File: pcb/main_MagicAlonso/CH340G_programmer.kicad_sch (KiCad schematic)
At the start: 13 parts, among them J2 USB_Out, J3 UART_Out, J4 USB_C_Receptacle_USB2.0_16P, Q1 NMOS, U4 CH340C

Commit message: schematic and test commit
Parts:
- D6: value 1N5819 -> SS14
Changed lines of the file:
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@@
 			)
 		)
-		(property "Value" "1N5819"
+		(property "Value" "SS14"
 			(at 91.694 26.67 0)
 			(effects

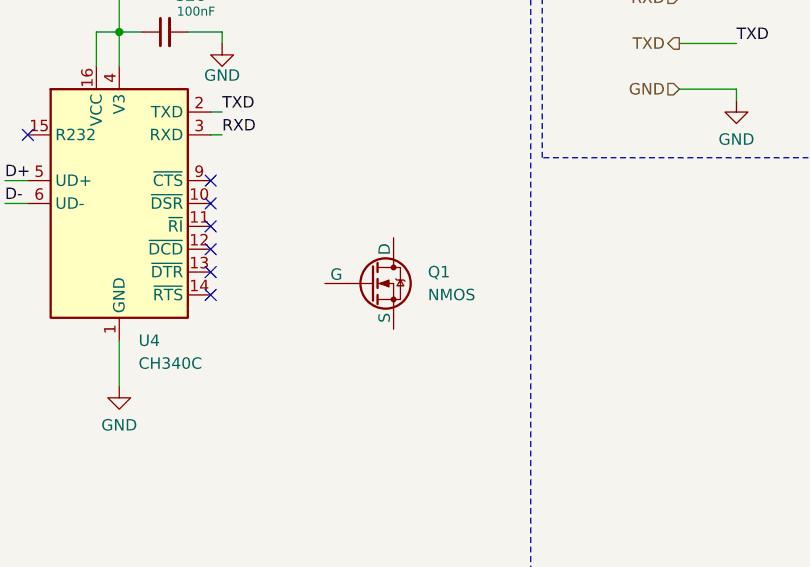
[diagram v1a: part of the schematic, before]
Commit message: Big changes PCB
Advancements on the schematic were made:
- Completed MP2315 circuit
- Passive Buzzer
- Mounting holes & other symbols added

Also the PCB drawings were improved.
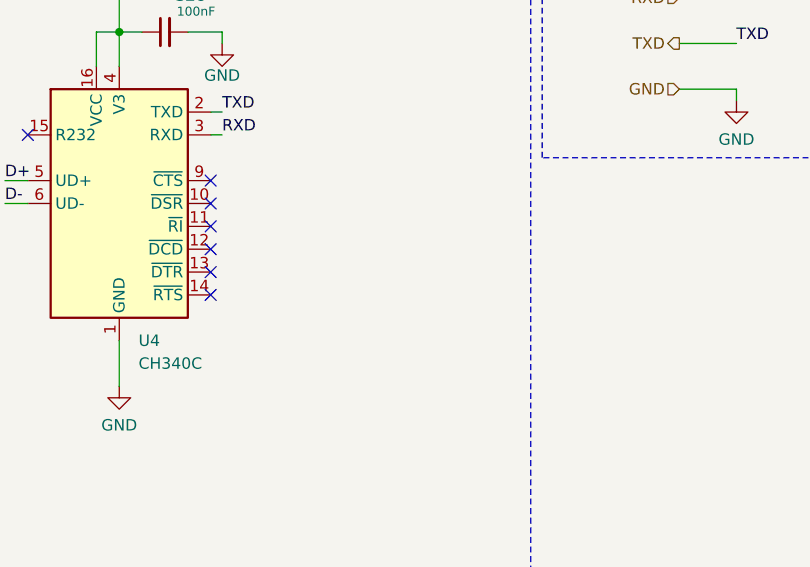
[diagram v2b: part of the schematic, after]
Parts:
- removed Q1: NMOS, symbol Simulation_SPICE:NMOS
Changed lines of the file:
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@@
-	)
-	(symbol
-		(lib_id "Simulation_SPICE:NMOS")
-		(at 170.18 68.58 0)
-		(unit 1)
-		(exclude_from_sim no)
-		(in_bom yes)
-		(on_board yes)
-		(dnp no)
-		(fields_autoplaced yes)
-		(property "Reference" "Q1"
-			(at 176.53 67.3099 0)
-			(effects
-				(font
-					(size 1.27 1.27)
-				)
-				(justify left)
-			)
-		)
-		(property "Value" "NMOS"
-			(at 176.53 69.8499 0)
-			(effects
-				(font
-					(size 1.27 1.27)
-				)
-				(justify left)
-			)
-		)
-		(property "Footprint" ""
-			(at 175.26 66.04 0)
-			(effects
-				(font
-					(size 1.27 1.27)
-				)
-				(hide yes)
-			)
-		)
-		(property "Datasheet" "https://ngspice.sourceforge.io/docs/ngspice-html-manual/manual.xhtml#cha_MOSFETs"
-			(at 170.18 81.28 0)
-			(effects
-				(font
-					(size 1.27 1.27)
-				)
-				(hide yes)
-			)
-		)
-		(property "Description" "N-MOSFET transistor, drain/source/gate"
-			(at 170.18 68.58 0)
-			(effects
-				(font
-					(size 1.27 1.27)
-				)
-				(hide yes)
-			)
-		)
-		(property "Sim.Device" "NMOS"
-			(at 170.18 85.725 0)
-			(effects
-				(font
-					(size 1.27 1.27)
-				)
-				(hide yes)
-			)
-		)
-		(property "Sim.Type" "VDMOS"
-			(at 170.18 87.63 0)
-			(effects
-				(font
-					(size 1.27 1.27)
-				)
-				(hide yes)
-			)
-		)
-		(property "Sim.Pins" "1=D 2=G 3=S"
-			(at 170.18 83.82 0)
-			(effects
-				(font
-					(size 1.27 1.27)
-				)
-				(hide yes)
-			)
-		)
-		(pin "1"
-		)
-		(pin "2"
-		)
-		(pin "3"
-		)
-		(instances
-			(project ""
-				(path "/80af5e1a-3060-4775-9fc3-f6762d1535e7/c19a4b5e-b66e-4d93-9513-18dbfa3808b4"
-					(reference "Q1")
-					(unit 1)
-				)
-			)
-		)
 	)
 	(symbol

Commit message: yes, schematic
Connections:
- no-connect marks 8 -> 10
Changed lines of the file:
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@@
+	)
+	(no_connect
+		(at 48.26 60.96)
 	)
 	(no_connect
@@
 		(at 152.4 57.15)
 	)
+	(no_connect
+		(at 48.26 63.5)
+	)
 	(wire

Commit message: schematic almost finished
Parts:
- added C13: 1uF, Capacitor_SMD:C_0603_1608Metric_Pad1.08x0.95mm_HandSolder, symbol Device:C_Small
- added D7: SS14, Diode_SMD:D_SMA, symbol Device:D_Schottky
- added J16: USB_B_Micro, symbol Connector:USB_B_Micro
- renumbered C16 to C14, C14 to C15, C15 to C16, J4 to J13, J3 to J14, J2 to J15, R4 to R10, R3 to R11, R5 to R12, R6 to R13
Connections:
- net +3.3V: now also C13.1
- net D+: now also J16.3 (D+)
- net D-: now also J16.2 (D-)
- net GND: now also C13.2, J16.5 (GND), J16.6 (Shield)
- net Vbus: no longer D6.2 (A), J13.A4 (VBUS), J13.A9 (VBUS), J13.B4 (VBUS), J13.B9 (VBUS)
- net Vusb: now also D7.1 (K)
- new net VbusB: D7.2 (A), J16.1 (VBUS)
- new net VbusC: D6.2 (A), J13.A4 (VBUS), J13.A9 (VBUS), J13.B4 (VBUS), J13.B9 (VBUS)
- no-connect marks 10 -> 11
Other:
- note added: "Aux USB Port"
- moved on the sheet: C14, C15, C16, D6, U4

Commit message: some footprint assignment
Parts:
- C14, C16: footprint Capacitor_SMD:C_0603_1608Metric_Pad1.08x0.95mm_HandSolder -> Capacitor_SMD:C_0805_2012Metric
- R10, R11, R12, R13: footprint (none) -> Resistor_SMD:R_0805_2012Metric
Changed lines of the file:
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@@
 			)
 		)
-		(property "Footprint" ""
+		(property "Footprint" "Resistor_SMD:R_0805_2012Metric"
 			(at 31.75 92.71 0)
 			(effects
@@
 			)
 		)
-		(property "Footprint" "Capacitor_SMD:C_0603_1608Metric_Pad1.08x0.95mm_HandSolder"
+		(property "Footprint" "Capacitor_SMD:C_0805_2012Metric"
 			(at 137.16 45.72 0)
 			(effects
@@
 			)
 		)
-		(property "Footprint" ""
+		(property "Footprint" "Resistor_SMD:R_0805_2012Metric"
 			(at 44.45 92.71 0)
 			(effects
@@
 			)
 		)
-		(property "Footprint" ""
+		(property "Footprint" "Resistor_SMD:R_0805_2012Metric"
 			(at 34.29 92.71 0)
 			(effects
@@
 			)
 		)
-		(property "Footprint" "Capacitor_SMD:C_0603_1608Metric_Pad1.08x0.95mm_HandSolder"
+		(property "Footprint" "Capacitor_SMD:C_0805_2012Metric"
 			(at 90.17 46.99 0)
 			(effects
@@
 			)
 		)
-		(property "Footprint" ""
+		(property "Footprint" "Resistor_SMD:R_0805_2012Metric"
 			(at 46.99 92.71 0)
 			(effects

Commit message: footprint assingment completed
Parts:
- J13: footprint (none) -> Connector_USB:USB_C_Receptacle_GCT_USB4110
- J14: footprint (none) -> Connector_JST:JST_XH_B4B-XH-AM_1x04_P2.50mm_Vertical
- J15: footprint (none) -> Connector_JST:JST_XH_B2B-XH-AM_1x02_P2.50mm_Vertical
- J16: footprint (none) -> Connector_USB:USB_Micro-B_Amphenol_10104110_Horizontal
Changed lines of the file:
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@@
 			)
 		)
-		(property "Footprint" ""
+		(property "Footprint" "Connector_USB:USB_Micro-B_Amphenol_10104110_Horizontal"
 			(at 30.48 134.62 0)
 			(effects
@@
 			)
 		)
-		(property "Footprint" ""
+		(property "Footprint" "Connector_JST:JST_XH_B2B-XH-AM_1x02_P2.50mm_Vertical"
 			(at 89.408 93.726 0)
 			(effects
@@
 			)
 		)
-		(property "Footprint" ""
+		(property "Footprint" "Connector_USB:USB_C_Receptacle_GCT_USB4110"
 			(at 36.83 48.26 0)
 			(effects
@@
 			)
 		)
-		(property "Footprint" ""
+		(property "Footprint" "Connector_JST:JST_XH_B4B-XH-AM_1x04_P2.50mm_Vertical"
 			(at 88.9 77.47 0)
 			(effects

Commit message: pcb footprint added
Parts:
- J15: footprint Connector_JST:JST_XH_B2B-XH-AM_1x02_P2.50mm_Vertical -> Connector_JST:JST_XH_B5B-XH-AM_1x05_P2.50mm_Vertical
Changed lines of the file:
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@@
 			)
 		)
-		(property "Footprint" "Connector_JST:JST_XH_B2B-XH-AM_1x02_P2.50mm_Vertical"
+		(property "Footprint" "Connector_JST:JST_XH_B5B-XH-AM_1x05_P2.50mm_Vertical"
 			(at 89.408 93.726 0)
 			(effects

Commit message: pcb components & label fixes
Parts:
- C15: footprint Capacitor_Tantalum_SMD:CP_EIA-3216-10_Kemet-I_Pad1.58x1.35mm_HandSolder -> Capacitor_Tantalum_SMD:CP_EIA-3216-10_Kemet-I_HandSolder
- J14: footprint Connector_JST:JST_XH_B4B-XH-AM_1x04_P2.50mm_Vertical -> Connector_JST:JST_XH_B4B-XH-A_1x04_P2.50mm_Vertical
- J15: footprint Connector_JST:JST_XH_B5B-XH-AM_1x05_P2.50mm_Vertical -> Connector_PinSocket_2.54mm:PinSocket_1x05_P2.54mm_Vertical
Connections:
- net Vbus renamed VMus
- net VbusB renamed VMusB
- net VbusC renamed VMusC
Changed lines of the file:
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@@
 		)
 	)
-	(label "VbusC"
+	(label "VMusC"
 		(at 80.01 29.21 180)
 		(effects
@@
 		)
 	)
-	(label "VbusB"
+	(label "VMusB"
 		(at 35.56 128.27 0)
 		(effects
@@
 		)
 	)
-	(label "VbusC"
+	(label "VMusC"
 		(at 49.53 33.02 0)
 		(effects
@@
 		)
 	)
-	(label "VbusB"
+	(label "VMusB"
 		(at 49.53 144.78 180)
 		(effects
@@
 		)
 	)
-	(label "Vbus"
+	(label "VMus"
 		(at 83.058 88.646 180)
 		(effects
@@
 			)
 		)
-		(property "Footprint" "Connector_JST:JST_XH_B5B-XH-AM_1x05_P2.50mm_Vertical"
+		(property "Footprint" "Connector_PinSocket_2.54mm:PinSocket_1x05_P2.54mm_Vertical"
 			(at 89.408 93.726 0)
 			(effects
@@
 			)
 		)
-		(property "Footprint" "Connector_JST:JST_XH_B4B-XH-AM_1x04_P2.50mm_Vertical"
+		(property "Footprint" "Connector_JST:JST_XH_B4B-XH-A_1x04_P2.50mm_Vertical"
 			(at 88.9 77.47 0)
 			(effects
@@
 			)
 		)
-		(property "Footprint" "Capacitor_Tantalum_SMD:CP_EIA-3216-10_Kemet-I_Pad1.58x1.35mm_HandSolder"
+		(property "Footprint" "Capacitor_Tantalum_SMD:CP_EIA-3216-10_Kemet-I_HandSolder"
 			(at 85.09 46.99 0)
 			(effects
